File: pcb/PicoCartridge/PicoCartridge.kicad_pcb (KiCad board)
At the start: 4 copper layers, 51 x 30.7 mm, 38 parts, among them J1 GameBoy_GamePak_AGB-002, J301 DBG, J401 Micro_SD_Card, U1 RP2350B-QFN80, U2 W25Q128JVS, U3 MCP7940N-xSN

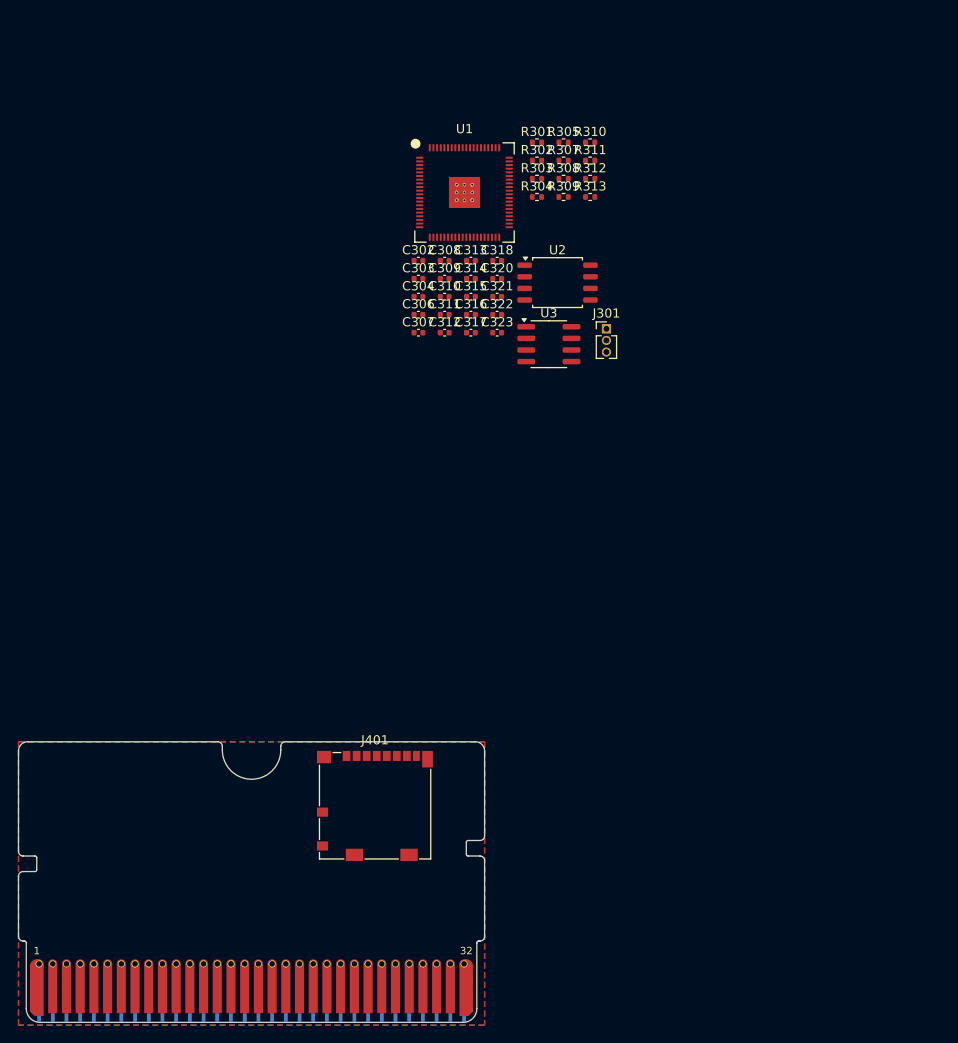
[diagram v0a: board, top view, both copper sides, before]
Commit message: Fixed connection between MCU and SD card
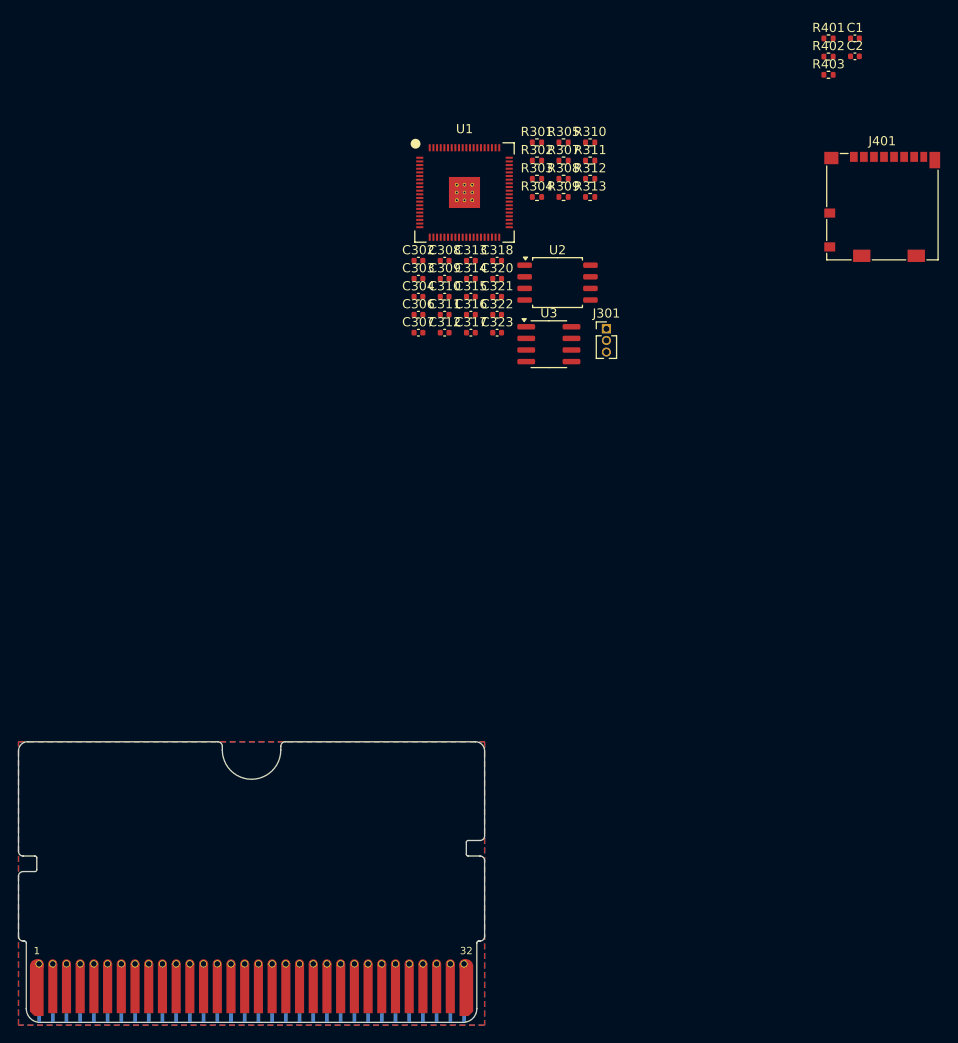
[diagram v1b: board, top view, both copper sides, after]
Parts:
- added C1: 4.7u, Capacitor_SMD:C_0402_1005Metric, F.Cu at (191.5, 23.0)
- added C2: 4.7u, Capacitor_SMD:C_0402_1005Metric, F.Cu at (191.5, 25.0)
- added R401: 10k, Resistor_SMD:R_0402_1005Metric, F.Cu at (188.6, 23.0)
- added R402: 10k, Resistor_SMD:R_0402_1005Metric, F.Cu at (188.6, 25.0)
- added R403: 10k, Resistor_SMD:R_0402_1005Metric, F.Cu at (188.6, 27.0)
- moved J401 85.9 mm to (194.5, 41.5)
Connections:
- J401 pad 1: unconnected-(J401-DAT2-Pad1) -> /MCU/SD_DAT2
- J401 pad 2: unconnected-(J401-DAT3/CD-Pad2) -> /MCU/~{SPI0_CS}
- J401 pad 3: unconnected-(J401-CMD-Pad3) -> /MCU/SPI0_TX
- J401 pad 4: unconnected-(J401-VDD-Pad4) -> +3.3V
- J401 pad 5: unconnected-(J401-CLK-Pad5) -> /MCU/SPI0_SCLK
- J401 pad 7: unconnected-(J401-DAT0-Pad7) -> /MCU/SPI0_RX
- J401 pad 8: unconnected-(J401-DAT1-Pad8) -> /MCU/SD_DAT1

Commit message: Fixed GBA bus internal logic
THe GBA bus is now a correct bus in a sense of kicad
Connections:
- net /GBA Bus/GBA_Bus_A00 renamed /GBA Bus/GbaDataBus_A00
- net /GBA Bus/GBA_Bus_A01 renamed /GBA Bus/GbaDataBus_A01
- net /GBA Bus/GBA_Bus_A02 renamed /GBA Bus/GbaDataBus_A02
- net /GBA Bus/GBA_Bus_A03 renamed /GBA Bus/GbaDataBus_A03
- net /GBA Bus/GBA_Bus_A04 renamed /GBA Bus/GbaDataBus_A04
- net /GBA Bus/GBA_Bus_A05 renamed /GBA Bus/GbaDataBus_A05
- net /GBA Bus/GBA_Bus_A06 renamed /GBA Bus/GbaDataBus_A06
- net /GBA Bus/GBA_Bus_A07 renamed /GBA Bus/GbaDataBus_A07
- net /GBA Bus/GBA_Bus_A08 renamed /GBA Bus/GbaDataBus_A08
- net /GBA Bus/GBA_Bus_A09 renamed /GBA Bus/GbaDataBus_A09
- net /MCU/GBA_Bus_A00 renamed /MCU/GbaDataBus_A00
- net /MCU/GBA_Bus_A01 renamed /MCU/GbaDataBus_A01
- net /MCU/GBA_Bus_A02 renamed /MCU/GbaDataBus_A02
- net /MCU/GBA_Bus_A03 renamed /MCU/GbaDataBus_A03
- net /MCU/GBA_Bus_A04 renamed /MCU/GbaDataBus_A04
- net /MCU/GBA_Bus_A05 renamed /MCU/GbaDataBus_A05
- net /MCU/GBA_Bus_A06 renamed /MCU/GbaDataBus_A06
- net /MCU/GBA_Bus_A07 renamed /MCU/GbaDataBus_A07
- net /MCU/GBA_Bus_A08 renamed /MCU/GbaDataBus_A08
- net /MCU/GBA_Bus_A09 renamed /MCU/GbaDataBus_A09
- net /MCU/MFP renamed /GBA Bus/MFP
- J1 pad 16: /GBA Bus/GBA_Bus_A10 -> /GBA Bus/GbaDataBus_A10
- J1 pad 17: /GBA Bus/GBA_Bus_A11 -> /GBA Bus/GbaDataBus_A11
- J1 pad 18: /GBA Bus/GBA_Bus_A12 -> /GBA Bus/GbaDataBus_A12
- J1 pad 19: /GBA Bus/GBA_Bus_A13 -> /GBA Bus/GbaDataBus_A13
- J1 pad 20: /GBA Bus/GBA_Bus_A14 -> /GBA Bus/GbaDataBus_A14
- J1 pad 21: /GBA Bus/GBA_Bus_A15 -> /GBA Bus/GbaDataBus_A15
- J1 pad 22: /GBA Bus/GBA_Bus_D00 -> /GBA Bus/GbaDataBus_D0
- J1 pad 23: /GBA Bus/GBA_Bus_D01 -> /GBA Bus/GbaDataBus_D1
- J1 pad 24: /GBA Bus/GBA_Bus_D02 -> /GBA Bus/GbaDataBus_D2
- J1 pad 25: /GBA Bus/GBA_Bus_D03 -> /GBA Bus/GbaDataBus_D3
- J1 pad 26: /GBA Bus/GBA_Bus_D04 -> /GBA Bus/GbaDataBus_D4
- J1 pad 27: /GBA Bus/GBA_Bus_D05 -> /GBA Bus/GbaDataBus_D5
- J1 pad 28: /GBA Bus/GBA_Bus_D06 -> /GBA Bus/GbaDataBus_D6
- J1 pad 29: /GBA Bus/GBA_Bus_D07 -> /GBA Bus/GbaDataBus_D7
- J1 pad 3: /GBA Bus/~{GBA_Bus_WR} -> /MCU/~{GBA_Bus_WR}
- J1 pad 30: /GBA Bus/~{GBA_Bus_CS2} -> /MCU/~{GBA_Bus_CS2}
- J1 pad 31: /GBA Bus/GBA_Bus_IRQ -> /MCU/GBA_Bus_IRQ
- J1 pad 4: /GBA Bus/~{GBA_Bus_RD} -> /MCU/~{GBA_Bus_RD}
- J1 pad 5: /GBA Bus/~{GBA_Bus_CS} -> /MCU/~{GBA_Bus_CS}
- U1 pad 18: /MCU/GBA_Bus_A10 -> /GBA Bus/GbaDataBus_A10
- U1 pad 19: /MCU/GBA_Bus_A11 -> /GBA Bus/GbaDataBus_A11
- U1 pad 20: /MCU/GBA_Bus_A12 -> /GBA Bus/GbaDataBus_A12
- U1 pad 21: /MCU/GBA_Bus_A13 -> /GBA Bus/GbaDataBus_A13
- U1 pad 22: /MCU/GBA_Bus_A14 -> /GBA Bus/GbaDataBus_A14
- U1 pad 23: /MCU/GBA_Bus_A15 -> /GBA Bus/GbaDataBus_A15
- U1 pad 25: /MCU/GBA_Bus_D00 -> /GBA Bus/GbaDataBus_D0
- U1 pad 26: /MCU/GBA_Bus_D01 -> /GBA Bus/GbaDataBus_D1
- U1 pad 27: /MCU/GBA_Bus_D02 -> /GBA Bus/GbaDataBus_D2
- U1 pad 28: /MCU/GBA_Bus_D03 -> /GBA Bus/GbaDataBus_D3
- U1 pad 36: /MCU/GBA_Bus_D04 -> /GBA Bus/GbaDataBus_D4
- U1 pad 37: /MCU/GBA_Bus_D05 -> /GBA Bus/GbaDataBus_D5
- U1 pad 38: /MCU/GBA_Bus_D06 -> /GBA Bus/GbaDataBus_D6
- U1 pad 39: /MCU/GBA_Bus_D07 -> /GBA Bus/GbaDataBus_D7

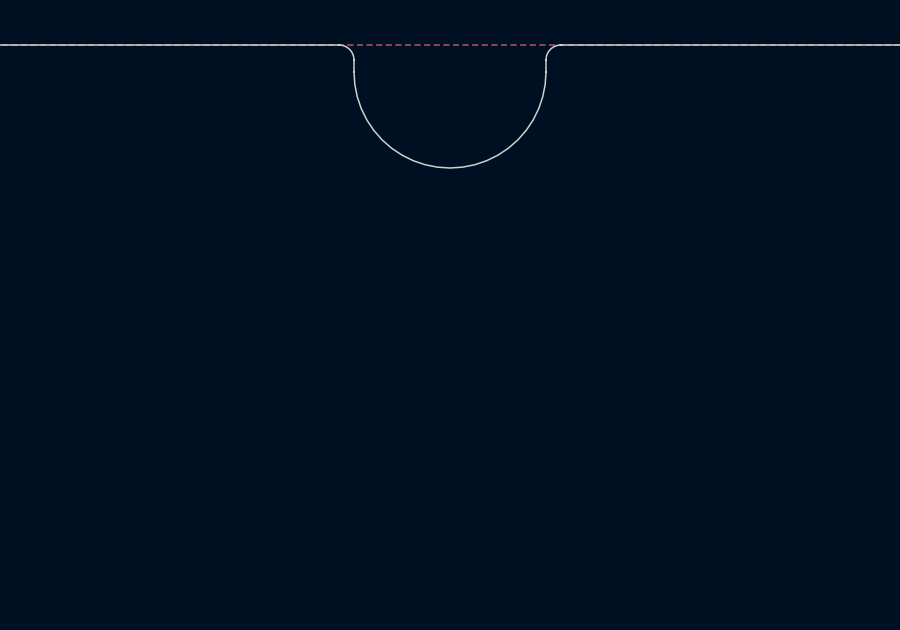
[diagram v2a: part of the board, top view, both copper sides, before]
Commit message: Added programmer connection (#4)
* Removed dedicated usb connector

Use would be very limited (live view on a pc and data transfer without
removing the sd card) and increases the pcb & schematic complexity by a lot.

Removing the usb connector for this revision. It is possible, if this design
is successful that I will create a new revision at some point. You never know.

* Added programmer "connector"

Additionally removed reset and program switches as there is no need for
them on the pcb itself if there is no usb connection.
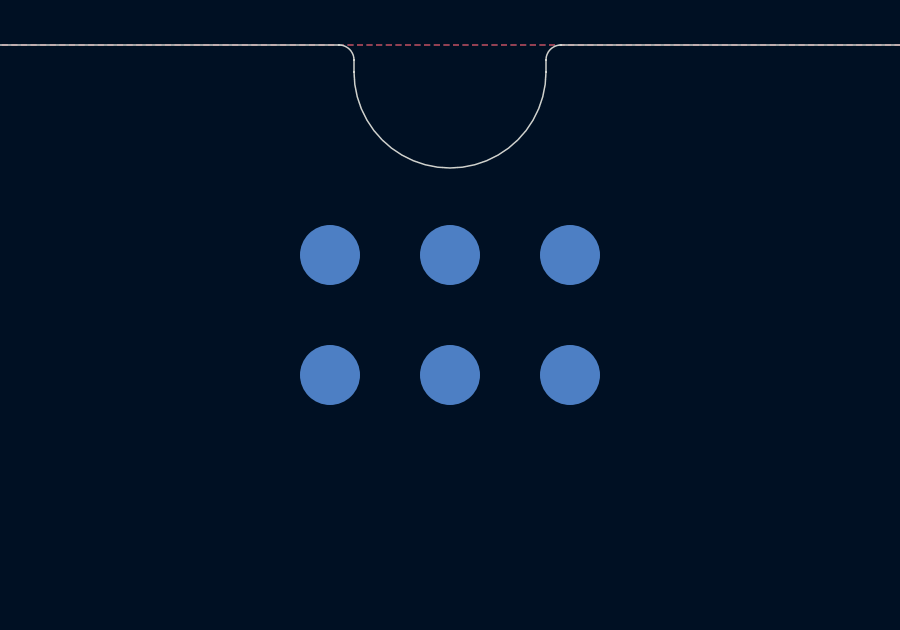
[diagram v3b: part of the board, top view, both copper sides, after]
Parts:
- added J302: ~, PicoCartridge:ProgrammerConnector_SMD, F.Cu at (125.5, 109.0)
- added REF**: WEEE-Logo_4.2x6mm_SilkScreen, Symbol:WEEE-Logo_4.2x6mm_SilkScreen, B.Cu at (146.5, 110.5)
- added REF**: KiCad-Logo2_5mm_SilkScreen, Symbol:KiCad-Logo2_5mm_SilkScreen, B.Cu at (144.0, 103.5)
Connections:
- R304 pad 1: /MCU/~{USB_BOOT} -> /MCU/~{RESET}
- R307 pad 2: /MCU/USB_DP -> /MCU/UsbDP
- R308 pad 2: /MCU/USB_DM -> /MCU/UsbDM
- U1 pad 58: /MCU/USB_PWR_DET -> unconnected-(U1-GPIO47_ADC7-Pad58)
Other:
- board text added: "DM !RESET GND DP !MODE 3.3"
- board text added: "Programmer"

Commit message: Upload progress
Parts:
- added Y302: Crystal, Crystal:Crystal_DS26_D2.0mm_L6.0mm_Horizontal, F.Cu at (139.2, 114.9)
- moved J401 84.3 mm to (141.5, 107.0)
- moved U2 75.8 mm to (106.0, 104.0)
- moved U1 75.8 mm to (120.0, 110.0), turned to 45 degrees
- moved C314 71.4 mm to (123.7, 115.9), turned to -135 degrees
- moved C310 65.3 mm to (126.0, 113.3), turned to 45 degrees
- moved C313 64.2 mm to (127.6, 107.8), turned to 45 degrees
- moved C323 62.8 mm to (141.0, 117.0), turned to 90 degrees
- moved C322 62.5 mm to (141.0, 114.8), turned to -90 degrees
- moved U3 61.9 mm to (145.5, 117.1)
- moved C311 56.3 mm to (124.0, 104.8), turned to 135 degrees
- moved C312 54.6 mm to (125.3, 105.5), turned to 45 degrees
- moved REF** 42.5 mm to (104.0, 110.5)
- moved REF** 37.0 mm to (107.0, 103.5)
- moved J302 15.6 mm to (141.0, 107.0)
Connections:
- J1 pad 10: /GBA Bus/GbaDataBus_A04 -> /GBA Bus/GbaDataBus_A4
- J1 pad 11: /GBA Bus/GbaDataBus_A05 -> /GBA Bus/GbaDataBus_A5
- J1 pad 12: /GBA Bus/GbaDataBus_A06 -> /GBA Bus/GbaDataBus_A6
- J1 pad 13: /GBA Bus/GbaDataBus_A07 -> /GBA Bus/GbaDataBus_A7
- J1 pad 14: /GBA Bus/GbaDataBus_A08 -> /GBA Bus/GbaDataBus_A8
- J1 pad 15: /GBA Bus/GbaDataBus_A09 -> /GBA Bus/GbaDataBus_A9
- J1 pad 6: /GBA Bus/GbaDataBus_A00 -> /GBA Bus/GbaDataBus_A0
- J1 pad 7: /GBA Bus/GbaDataBus_A01 -> /GBA Bus/GbaDataBus_A1
- J1 pad 8: /GBA Bus/GbaDataBus_A02 -> /GBA Bus/GbaDataBus_A2
- J1 pad 9: /GBA Bus/GbaDataBus_A03 -> /GBA Bus/GbaDataBus_A3
- U1 pad 11: /MCU/GbaDataBus_A04 -> /GBA Bus/GbaDataBus_A4
- U1 pad 12: /MCU/GbaDataBus_A05 -> /GBA Bus/GbaDataBus_A5
- U1 pad 13: /MCU/GbaDataBus_A06 -> /GBA Bus/GbaDataBus_A6
- U1 pad 14: /MCU/GbaDataBus_A07 -> /GBA Bus/GbaDataBus_A7
- U1 pad 16: /MCU/GbaDataBus_A08 -> /GBA Bus/GbaDataBus_A8
- U1 pad 17: /MCU/GbaDataBus_A09 -> /GBA Bus/GbaDataBus_A9
- U1 pad 6: /MCU/GbaDataBus_A00 -> /GBA Bus/GbaDataBus_A0
- U1 pad 7: /MCU/GbaDataBus_A01 -> /GBA Bus/GbaDataBus_A1
- U1 pad 8: /MCU/GbaDataBus_A02 -> /GBA Bus/GbaDataBus_A2
- U1 pad 9: /MCU/GbaDataBus_A03 -> /GBA Bus/GbaDataBus_A3
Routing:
- net /GBA Bus/GbaDataBus_D7: track 0.00 -> 25.1 mm, vias 0 -> 1
- net /GBA Bus/GbaDataBus_D5: track 0.00 -> 23.9 mm, vias 0 -> 1
- net /GBA Bus/GbaDataBus_D6: track 0.00 -> 23.8 mm, vias 0 -> 1
- net /GBA Bus/GbaDataBus_D4: track 0.00 -> 22.7 mm, vias 0 -> 1
- net /GBA Bus/GbaDataBus_D3: track 0.00 -> 22.2 mm, vias 0 -> 1
- net /GBA Bus/GbaDataBus_D2: track 0.00 -> 19.5 mm, vias 0 -> 1
- net /GBA Bus/GbaDataBus_D0: track 0.00 -> 18.7 mm, vias 0 -> 1
- net /MCU/~{GBA_Bus_WR}: track 0.00 -> 18.5 mm, vias 0 -> 1
- net /GBA Bus/GbaDataBus_D1: track 0.00 -> 18.2 mm, vias 0 -> 1
- net /GBA Bus/GbaDataBus_A15: track 0.00 -> 17.6 mm, vias 0 -> 1
- net /MCU/~{GBA_Bus_CS}: track 0.00 -> 17.0 mm, vias 0 -> 1
- net /MCU/~{GBA_Bus_RD}: track 0.00 -> 16.1 mm, vias 0 -> 1
- net /GBA Bus/GbaDataBus_A0: track 0.00 -> 16.1 mm, vias 0 -> 1
- net /GBA Bus/GbaDataBus_A3: track 0.00 -> 15.1 mm, vias 0 -> 1
- net /MCU/QSPI_SD1: track 0.00 -> 14.9 mm
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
